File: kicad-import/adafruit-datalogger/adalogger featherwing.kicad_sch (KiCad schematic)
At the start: 19 parts, among them IC3 PCF8523T, X4 microsd, Y2 32khz

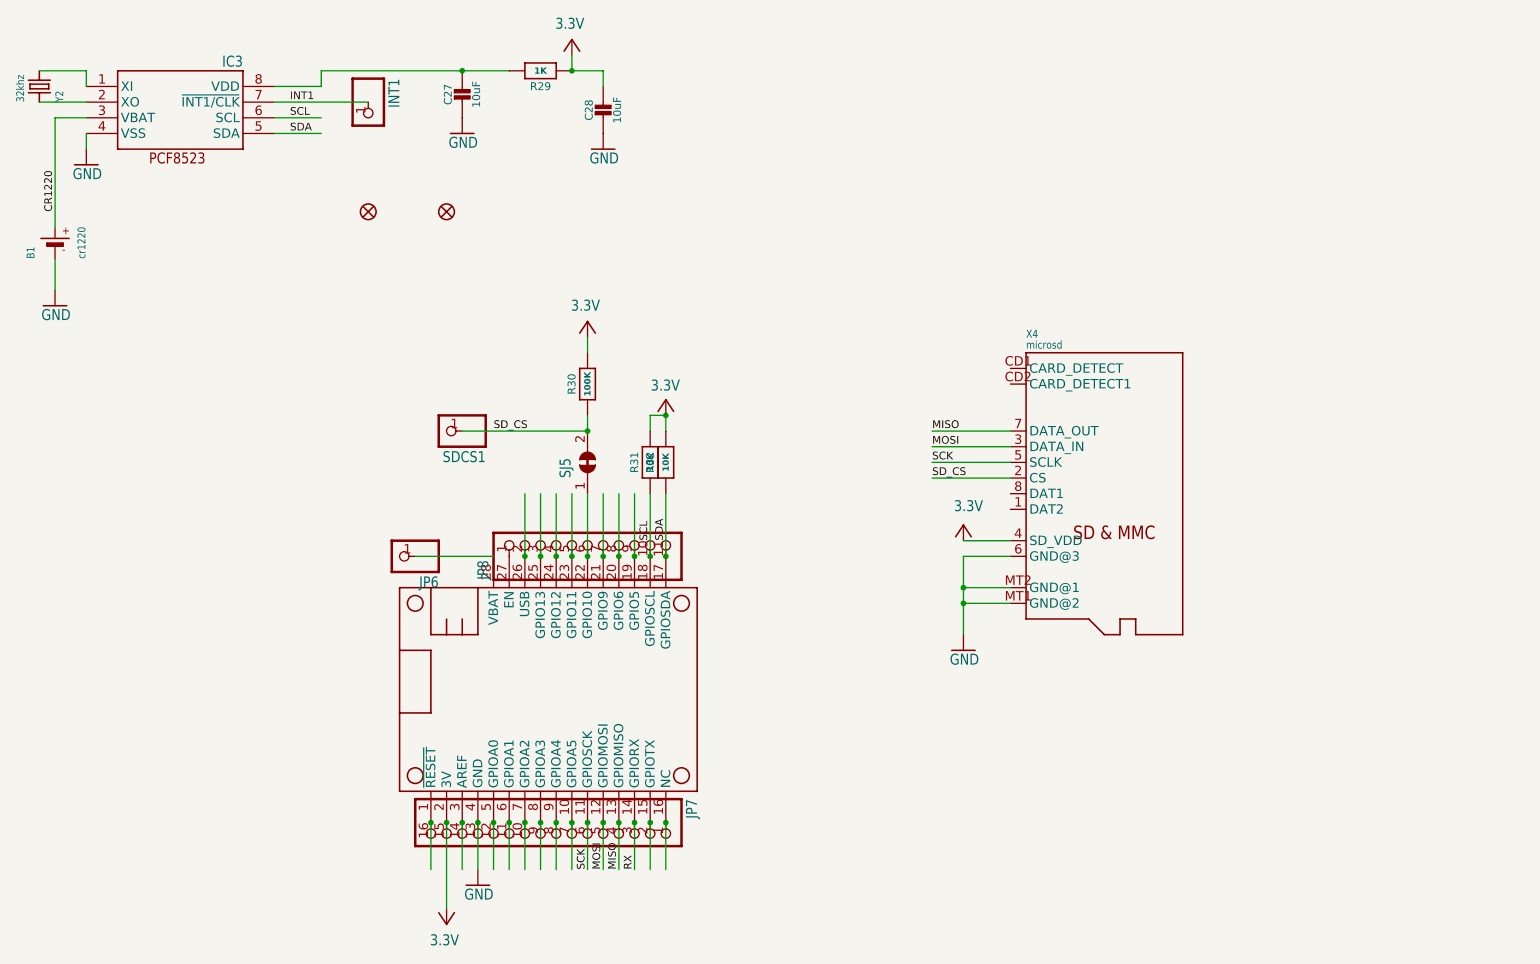
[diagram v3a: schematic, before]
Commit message: Start adding heirarchical labels. Add notes to check sub-feather jumpers.
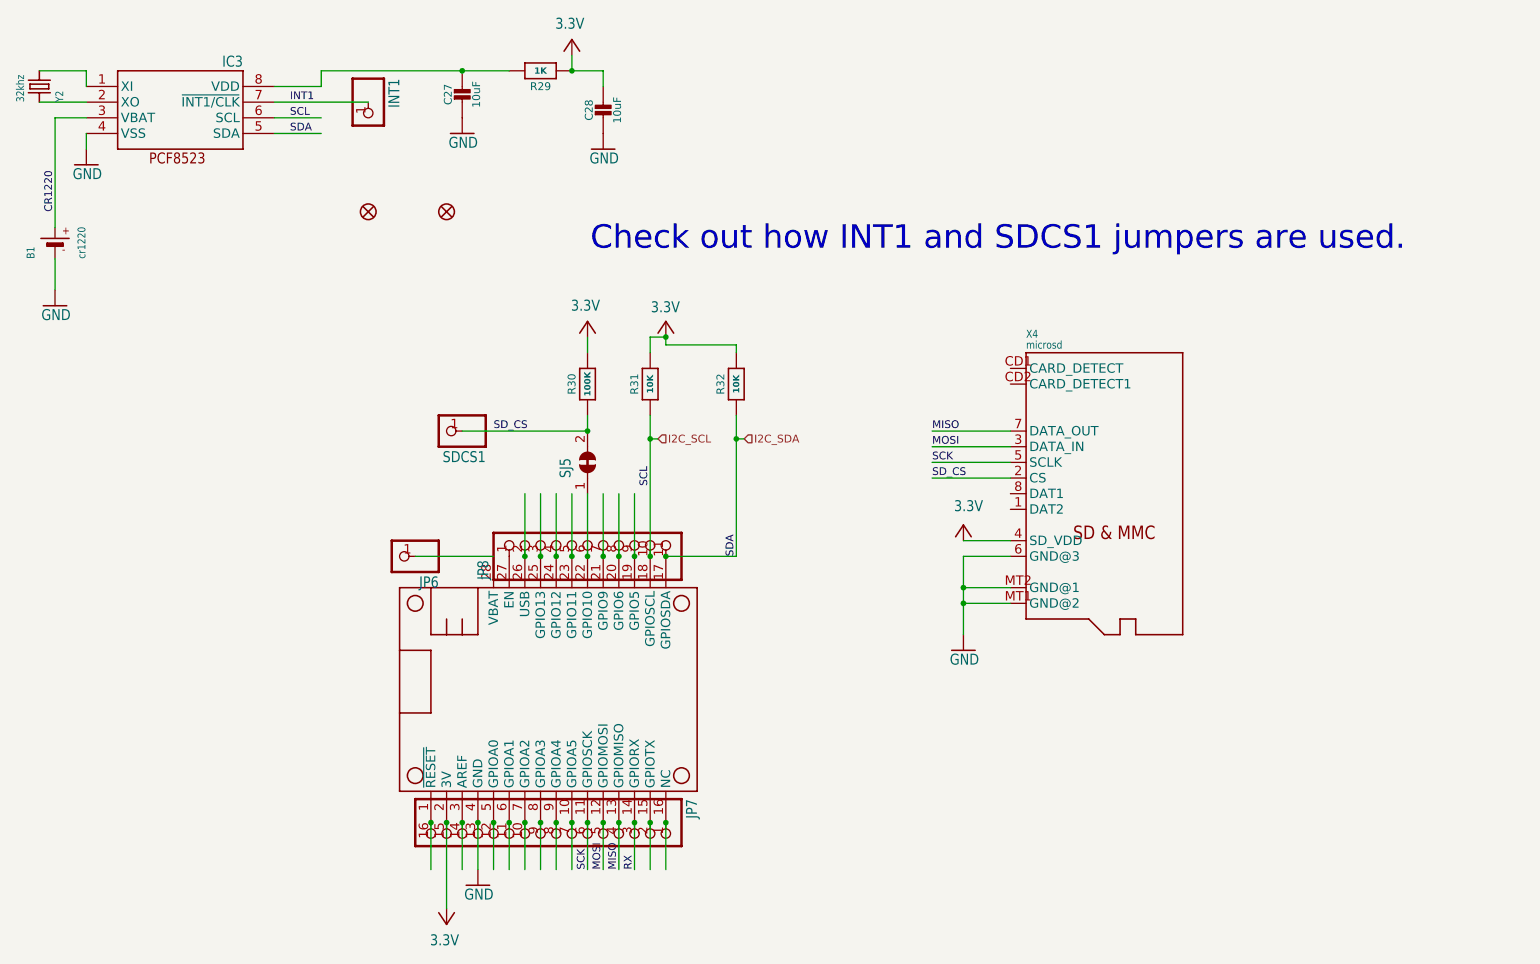
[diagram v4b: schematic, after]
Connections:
- net SCL renamed I2C_SCL
- net SDA renamed I2C_SDA
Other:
- note added: "Check out how INT1 and SDCS1 jumpers are used."
- moved on the sheet: R31, R32
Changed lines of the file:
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@@
 	(generator_version "9.0")
 	(paper "User" 298.45 217.322)
+	(text "Check out how INT1 and SDCS1 jumpers are used."
+		(exclude_from_sim no)
+		(at 191.008 62.738 0)
+		(effects
+			(font
+				(size 3.81 3.81)
+			)
+		)
+	)
 	(junction
 		(at 116.84 114.3)
@@
 	)
 	(junction
+		(at 134.62 95.25)
+		(diameter 0)
+		(color 0 0 0 0)
+	)
+	(junction
 		(at 104.14 35.56)
 		(diameter 0)
@@
 	)
 	(junction
-		(at 137.16 91.44)
+		(at 148.59 95.25)
+		(diameter 0)
+		(color 0 0 0 0)
+	)
+	(junction
+		(at 137.16 78.74)
 		(diameter 0)
 		(color 0 0 0 0)
@@
 	(wire
 		(pts
+			(xy 148.59 80.01) (xy 137.16 80.01)
+		)
+		(stroke
+			(width 0.1524)
+			(type solid)
+		)
+	)
+	(wire
+		(pts
 			(xy 81.28 38.1) (xy 73.66 38.1)
 		)
@@
 	(wire
 		(pts
+			(xy 148.59 114.3) (xy 137.16 114.3)
+		)
+		(stroke
+			(width 0.1524)
+			(type solid)
+		)
+	)
+	(wire
+		(pts
 			(xy 185.42 114.3) (xy 185.42 119.38)
 		)
@@
 	(wire
 		(pts
-			(xy 134.62 91.44) (xy 134.62 93.98)
+			(xy 134.62 78.74) (xy 134.62 81.28)
 		)
 		(stroke
@@
 	(wire
 		(pts
+			(xy 137.16 80.01) (xy 137.16 78.74)
+		)
+		(stroke
+			(width 0.1524)
+			(type solid)
+		)
+	)
+	(wire
+		(pts
 			(xy 119.38 104.14) (xy 119.38 114.3)
 		)
@@
 	(wire
 		(pts
-			(xy 134.62 104.14) (xy 134.62 114.3)
-		)
-		(stroke
-			(width 0.1524)
-			(type solid)
-		)
-	)
-	(wire
-		(pts
 			(xy 43.18 35.56) (xy 43.18 38.1)
 		)
@@
 	(wire
 		(pts
-			(xy 137.16 91.44) (xy 137.16 93.98)
+			(xy 148.59 80.01) (xy 148.59 81.28)
 		)
 		(stroke
@@
 	(wire
 		(pts
-			(xy 193.04 99.06) (xy 180.34 99.06)
-		)
-		(stroke
-			(width 0.1524)
-			(type solid)
-		)
-	)
-	(wire
-		(pts
-			(xy 43.18 40.64) (xy 35.56 40.64)
-		)
-		(stroke
-			(width 0.1524)
-			(type solid)
-		)
-	)
-	(wire
-		(pts
-			(xy 73.66 40.64) (xy 88.9 40.64)
-		)
-		(stroke
-			(width 0.1524)
-			(type solid)
-		)
-	)
-	(wire
-		(pts
-			(xy 121.92 33.02) (xy 121.92 35.56)
+			(xy 148.59 95.25) (xy 149.86 95.25)
 		)
 		(stroke
@@
 	(wire
 		(pts
+			(xy 193.04 99.06) (xy 180.34 99.06)
+		)
+		(stroke
+			(width 0.1524)
+			(type solid)
+		)
+	)
+	(wire
+		(pts
+			(xy 43.18 40.64) (xy 35.56 40.64)
+		)
+		(stroke
+			(width 0.1524)
+			(type solid)
+		)
+	)
+	(wire
+		(pts
+			(xy 73.66 40.64) (xy 88.9 40.64)
+		)
+		(stroke
+			(width 0.1524)
+			(type solid)
+		)
+	)
+	(wire
+		(pts
+			(xy 121.92 33.02) (xy 121.92 35.56)
+		)
+		(stroke
+			(width 0)
+			(type default)
+		)
+	)
+	(wire
+		(pts
 			(xy 124.46 104.14) (xy 124.46 114.3)
 		)
@@
 	(wire
 		(pts
+			(xy 134.62 95.25) (xy 135.89 95.25)
+		)
+		(stroke
+			(width 0)
+			(type default)
+		)
+	)
+	(wire
+		(pts
+			(xy 134.62 95.25) (xy 134.62 114.3)
+		)
+		(stroke
+			(width 0.1524)
+			(type solid)
+		)
+	)
+	(wire
+		(pts
 			(xy 180.34 101.6) (xy 193.04 101.6)
 		)
@@
 	(wire
 		(pts
+			(xy 134.62 91.44) (xy 134.62 95.25)
+		)
+		(stroke
+			(width 0.1524)
+			(type solid)
+		)
+	)
+	(wire
+		(pts
 			(xy 101.6 171.45) (xy 101.6 157.48)
 		)
@@
 	(wire
 		(pts
+			(xy 148.59 95.25) (xy 148.59 114.3)
+		)
+		(stroke
+			(width 0.1524)
+			(type solid)
+		)
+	)
+	(wire
+		(pts
 			(xy 185.42 119.38) (xy 185.42 121.92)
 		)
@@
 	(wire
 		(pts
-			(xy 137.16 104.14) (xy 137.16 114.3)
+			(xy 148.59 91.44) (xy 148.59 95.25)
 		)
 		(stroke
@@
 	(wire
 		(pts
-			(xy 137.16 91.44) (xy 134.62 91.44)
+			(xy 137.16 78.74) (xy 134.62 78.74)
 		)
 		(stroke
@@
 	)
 	(label "SCL"
-		(at 134.62 111.76 90)
+		(at 134.62 102.87 90)
 		(effects
 			(font
@@
 	)
 	(label "SDA"
-		(at 137.16 111.76 90)
+		(at 148.59 114.3 90)
 		(effects
 			(font
@@
 			)
 			(justify left bottom)
+		)
+	)
+	(hierarchical_label "I2C_SDA"
+		(shape input)
+		(at 149.86 95.25 0)
+		(effects
+			(font
+				(size 1.27 1.27)
+			)
+			(justify left)
+		)
+	)
+	(hierarchical_label "I2C_SCL"
+		(shape input)
+		(at 135.89 95.25 0)
+		(effects
+			(font
+				(size 1.27 1.27)
+			)
+			(justify left)
 		)
 	)
@@
 	(symbol
 		(lib_id "adalogger featherwing-eagle-import:RESISTOR_0603_NOOUT")
-		(at 137.16 99.06 90)
+		(at 148.59 86.36 90)
 		(unit 1)
 		(exclude_from_sim no)
@@
 		(dnp no)
 		(property "Reference" "R32"
-			(at 134.62 99.06 0)
+			(at 146.05 86.36 0)
 			(effects
 				(font
@@
 		)
 		(property "Value" "10K"
-			(at 137.16 99.06 0)
+			(at 148.59 86.36 0)
 			(effects
 				(font
@@
 		)
 		(property "Footprint" "adalogger featherwing:0603-NO"
-			(at 137.16 99.06 0)
+			(at 148.59 86.36 0)
 			(effects
 				(font
@@
 		)
 		(property "Datasheet" ""
-			(at 137.16 99.06 0)
+			(at 148.59 86.36 0)
 			(effects
 				(font
@@
 		)
 		(property "Description" ""
-			(at 137.16 99.06 0)
+			(at 148.59 86.36 0)
 			(effects
 				(font
@@
 	(symbol
 		(lib_id "adalogger featherwing-eagle-import:RESISTOR_0603_NOOUT")
-		(at 134.62 99.06 90)
+		(at 134.62 86.36 90)
 		(unit 1)
 		(exclude_from_sim no)
@@
 		(dnp no)
 		(property "Reference" "R31"
-			(at 132.08 99.06 0)
+			(at 132.08 86.36 0)
 			(effects
 				(font
@@
 		)
 		(property "Value" "10K"
-			(at 134.62 99.06 0)
+			(at 134.62 86.36 0)
 			(effects
 				(font
@@
 		)
 		(property "Footprint" "adalogger featherwing:0603-NO"
-			(at 134.62 99.06 0)
+			(at 134.62 86.36 0)
 			(effects
 				(font
@@
 		)
 		(property "Datasheet" ""
-			(at 134.62 99.06 0)
+			(at 134.62 86.36 0)
 			(effects
 				(font
@@
 		)
 		(property "Description" ""
-			(at 134.62 99.06 0)
+			(at 134.62 86.36 0)
 			(effects
 				(font
@@
 	(symbol
 		(lib_id "adalogger featherwing-eagle-import:+3V3")
-		(at 137.16 88.9 0)
+		(at 137.16 76.2 0)
 		(mirror y)
 		(unit 1)
@@
 		(dnp no)
 		(property "Reference" "#+3V04"
-			(at 137.16 88.9 0)
+			(at 137.16 76.2 0)
 			(effects
 				(font
@@
 		)
 		(property "Value" "3.3V"
-			(at 139.446 87.63 0)
+			(at 139.446 74.93 0)
 			(effects
 				(font
@@
 		)
 		(property "Footprint" ""
-			(at 137.16 88.9 0)
+			(at 137.16 76.2 0)
 			(effects
 				(font
@@
 		)
 		(property "Datasheet" ""
-			(at 137.16 88.9 0)
+			(at 137.16 76.2 0)
 			(effects
 				(font
@@
 		)
 		(property "Description" ""
-			(at 137.16 88.9 0)
-			(effects
-				(font
+			(at 137.16 76.2 0)
+			(effects
+				(font

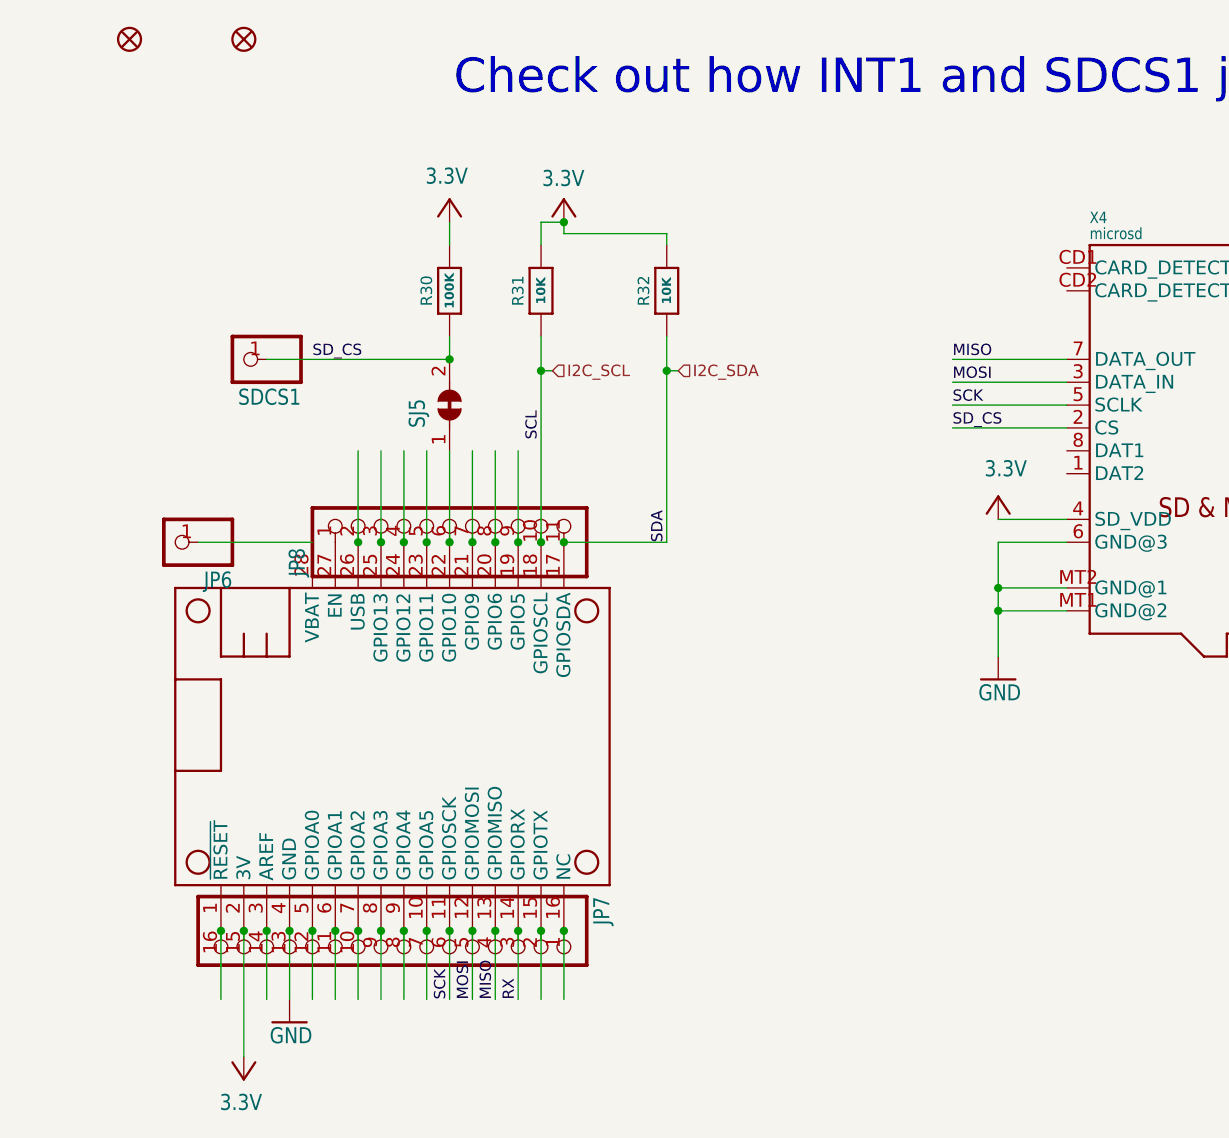
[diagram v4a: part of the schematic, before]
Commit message: Improve sheet labels. Remove extra model and headers from ETH and RTC pages.
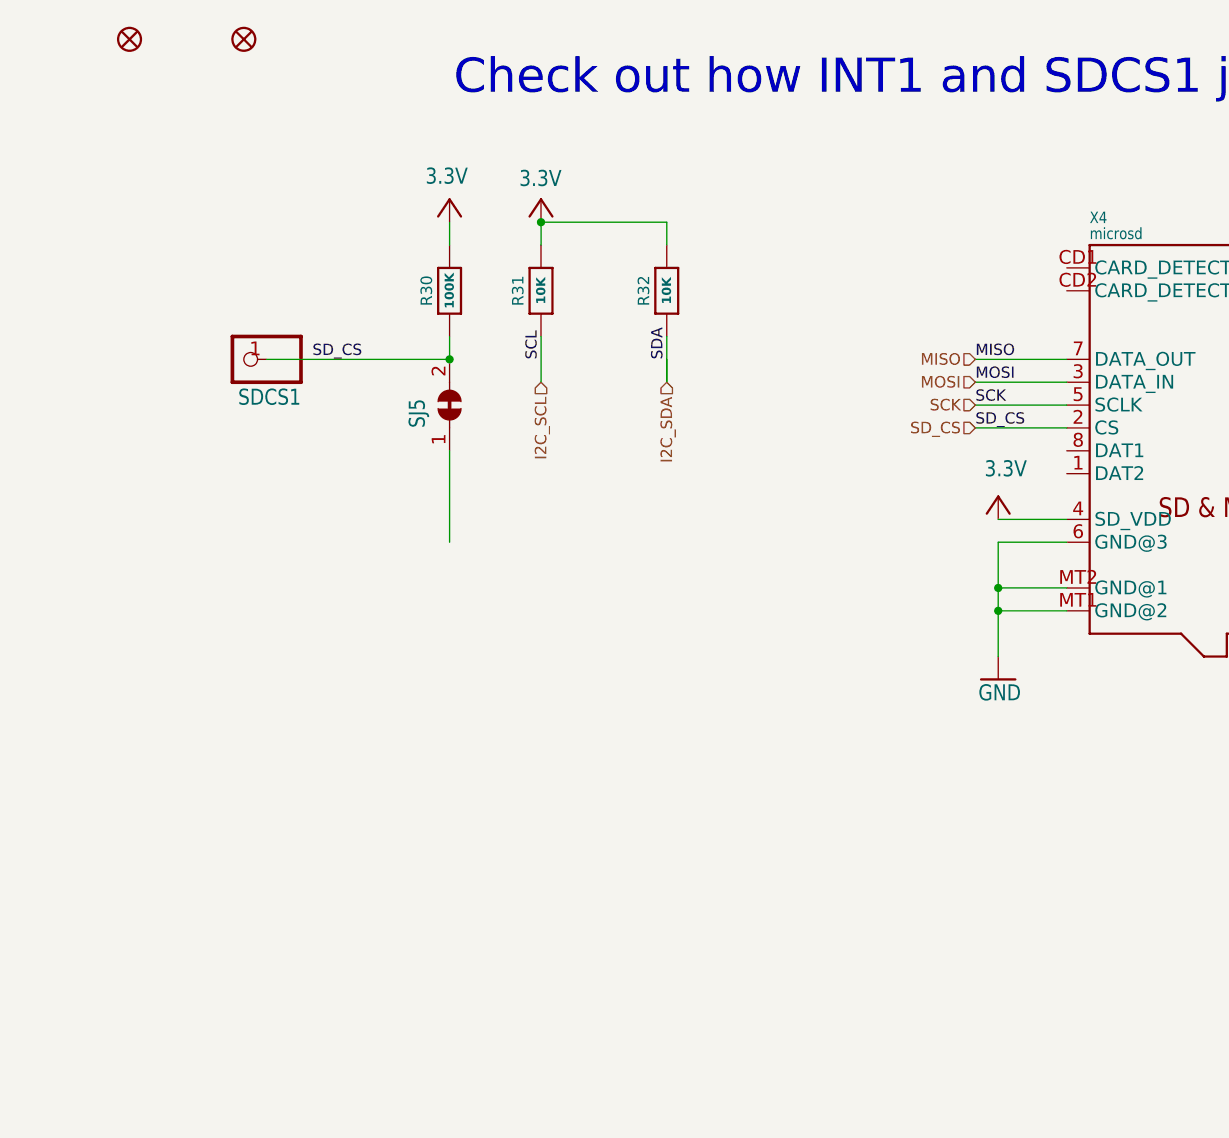
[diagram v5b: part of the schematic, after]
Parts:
- removed JP6: HEADER-1X1ROUND, adalogger featherwing:1X01_ROUND, symbol adalogger featherwing-eagle-import:HEADER-1X1ROUND
- removed JP7: HEADER-1X16ROUND, adalogger featherwing:1X16_ROUND, symbol adalogger featherwing-eagle-import:HEADER-1X16ROUND
- removed JP8: HEADER-1X11, adalogger featherwing:1X11_ROUND, symbol adalogger featherwing-eagle-import:HEADER-1X11
- removed MS2: FEATHERWING_NODIM, adalogger featherwing:FEATHERWING_NODIM, symbol adalogger featherwing-eagle-import:FEATHERWING_NODIM

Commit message: Some more net and label cleanup.
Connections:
- net SD_CS: now also SJ5.1
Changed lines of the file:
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@@
+	(wire
+		(pts
+			(xy 73.66 45.72) (xy 77.47 45.72)
+		)
+		(stroke
+			(width 0.1524)
+			(type solid)
+		)
+	)
 	(wire
 		(pts
@@
 	(wire
 		(pts
-			(xy 73.66 43.18) (xy 81.28 43.18)
+			(xy 73.66 43.18) (xy 77.47 43.18)
 		)
 		(stroke
@@
 		)
 	)
-	(wire
-		(pts
-			(xy 81.28 45.72) (xy 73.66 45.72)
-		)
-		(stroke
-			(width 0.1524)
-			(type solid)
-		)
-	)
 	(label "SDA"
-		(at 76.2 45.72 0)
+		(at 77.47 45.72 0)
 		(effects
 			(font
@@
 	)
 	(label "SCL"
-		(at 76.2 43.18 0)
+		(at 77.47 43.18 0)
 		(effects
 			(font
@@
 		)
 	)
+	(hierarchical_label "SCK"
+		(shape input)
+		(at 182.88 99.06 180)
+		(effects
+			(font
+				(size 1.27 1.27)
+			)
+			(justify right)
+		)
+	)
 	(hierarchical_label "SD_CS"
 		(shape input)
-		(at 182.88 101.6 180)
-		(effects
-			(font
-				(size 1.27 1.27)
-			)
-			(justify right)
-		)
-	)
-	(hierarchical_label "SCK"
-		(shape input)
-		(at 182.88 99.06 180)
-		(effects
-			(font
+		(at 124.46 114.3 270)
+		(effects
+			(font

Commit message: Initial sheet settings for layout.
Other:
- company: (none) -> Kingdom Metrics
- title: (none) -> Genesis Board
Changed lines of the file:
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@@
 	(generator_version "9.0")
 	(paper "User" 298.45 217.322)
+	(title_block
+		(title "Genesis Board")
+		(date "2025-05-27")
+		(rev "0.1")
+		(company "Kingdom Metrics")
+	)
 	(text "Check out how INT1 and SDCS1 jumpers are used."
 		(exclude_from_sim no)
